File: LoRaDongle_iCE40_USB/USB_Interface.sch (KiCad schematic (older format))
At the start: 25 parts

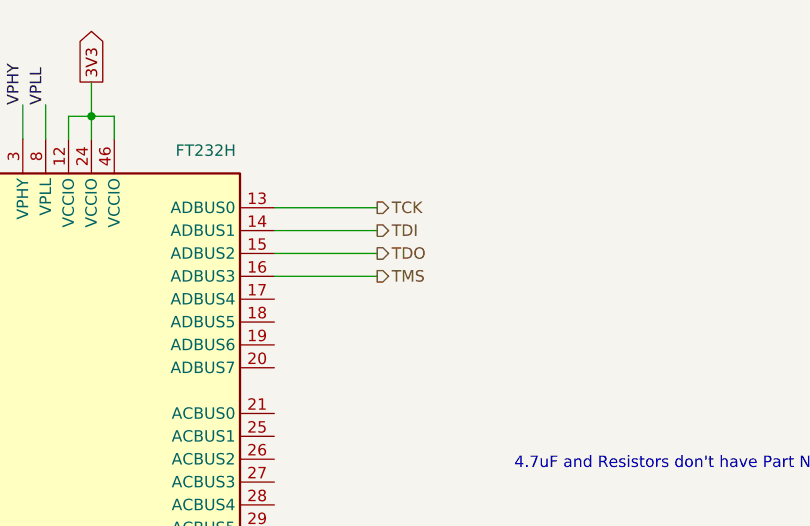
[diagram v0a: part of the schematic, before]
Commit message: initial changes to iCE40UP5k
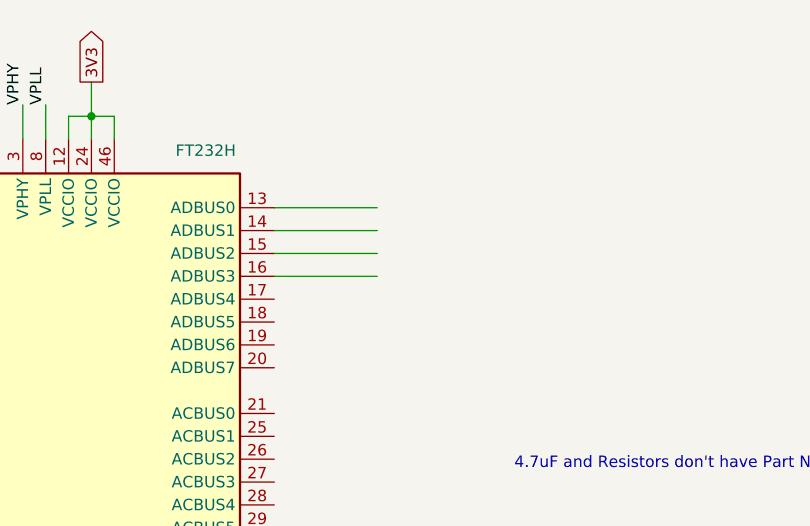
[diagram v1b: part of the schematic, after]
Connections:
- net labels removed: TCK, TDI, TDO, TMS
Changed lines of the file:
@@
 Wire Wire Line
 	7450 1900 7900 1900
-Text HLabel 7900 1600 2    50   Output ~ 0
-TCK
-Text HLabel 7900 1700 2    50   Output ~ 0
-TDI
-Text HLabel 7900 1800 2    50   Output ~ 0
-TDO
-Text HLabel 7900 1900 2    50   Output ~ 0
-TMS
 Text HLabel 5550 2200 0    50   Input ~ 0
 DM

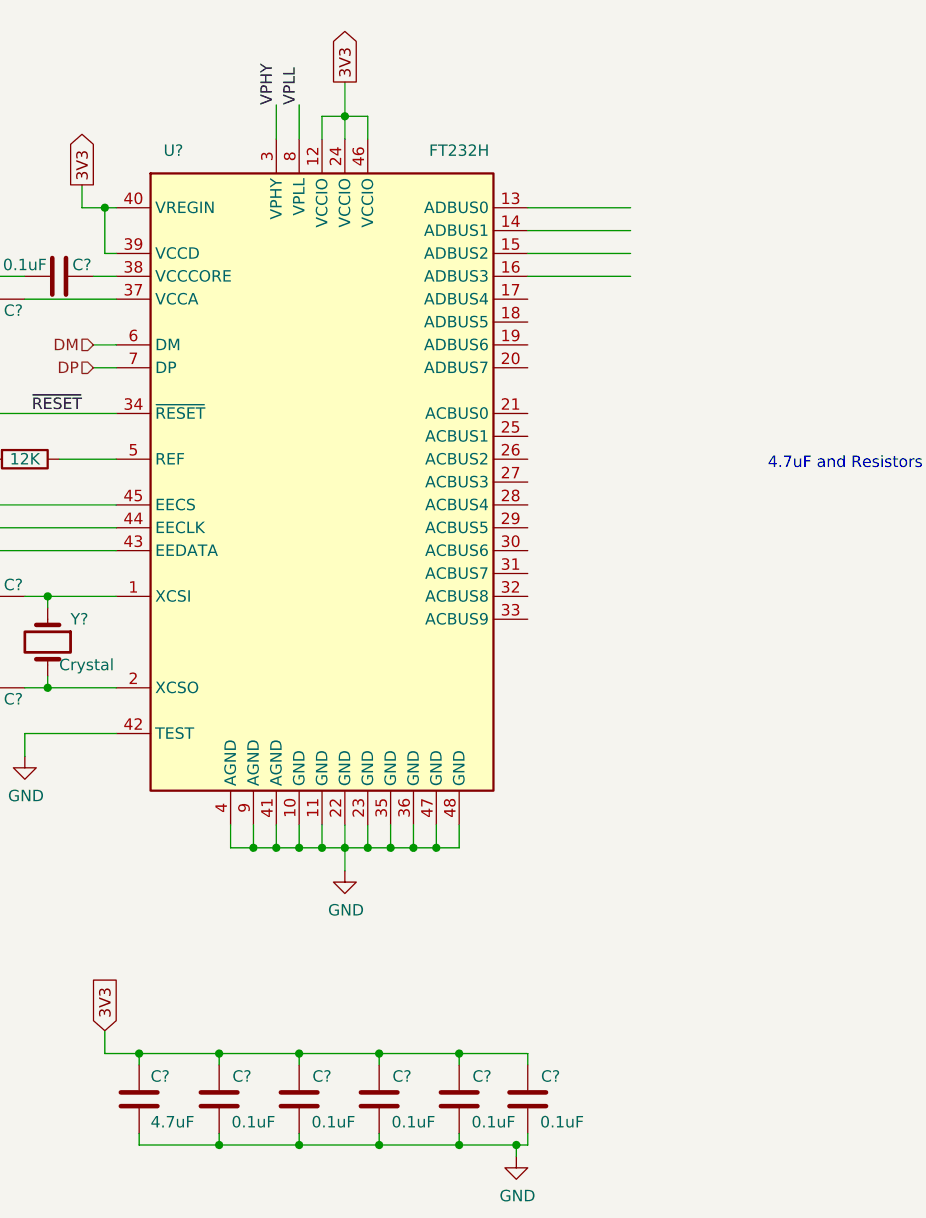
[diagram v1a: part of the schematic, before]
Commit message: changed to sx1261
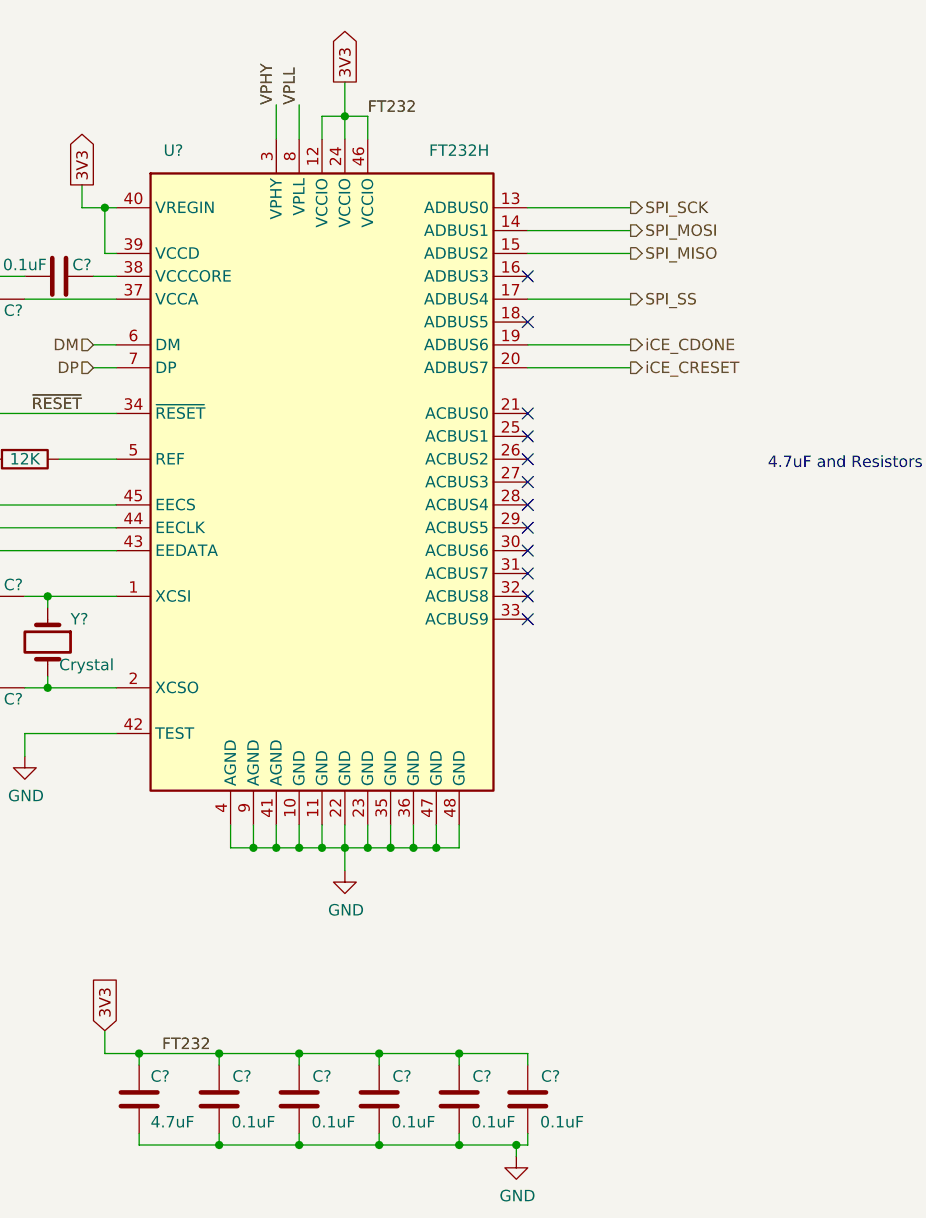
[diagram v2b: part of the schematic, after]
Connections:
- net labels added: FT232, SPI_MISO, SPI_MOSI, SPI_SCK, SPI_SS, iCE_CDONE, iCE_CRESET
- wire segments 129 -> 131
- no-connect marks 0 -> 12
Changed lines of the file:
@@
 $Descr A4 11693 8268
 encoding utf-8
-Sheet 5 5
+Sheet 4 5
 Title ""
 Date ""
@@
 Wire Wire Line
 	7450 1700 7900 1700
-Wire Wire Line
-	7450 1800 7900 1800
-Wire Wire Line
-	7450 1900 7900 1900
 Text HLabel 5550 2200 0    50   Input ~ 0
 DM
@@
 Text Notes 8500 2750 0    50   ~ 0
 4.7uF and Resistors don't have Part Numbers/footprints
+Text HLabel 7900 1600 2    50   Output ~ 0
+SPI_SCK
+Text HLabel 7900 1700 2    50   Output ~ 0
+SPI_MOSI
+Text HLabel 7900 1800 2    50   Output ~ 0
+SPI_MISO
+Text HLabel 7900 2000 2    50   Output ~ 0
+SPI_SS
+Text HLabel 7900 2200 2    50   Output ~ 0
+iCE_CDONE
+Text HLabel 7900 2300 2    50   Output ~ 0
+iCE_CRESET
+Wire Wire Line
+	7450 1800 7900 1800
+Wire Wire Line
+	7450 2000 7900 2000
+Wire Wire Line
+	7450 2200 7900 2200
+Wire Wire Line
+	7450 2300 7900 2300
+NoConn ~ 7450 2100
+NoConn ~ 7450 1900
+NoConn ~ 7450 2500
+NoConn ~ 7450 2600
+NoConn ~ 7450 2700
+NoConn ~ 7450 2800
+NoConn ~ 7450 2900
+NoConn ~ 7450 3000
+NoConn ~ 7450 3100
+NoConn ~ 7450 3200
+NoConn ~ 7450 3300
+NoConn ~ 7450 3400
+Text Label 6750 1200 0    50   ~ 0
+FT232
+Text Label 5850 5300 0    50   ~ 0
+FT232
 $EndSCHEMATC

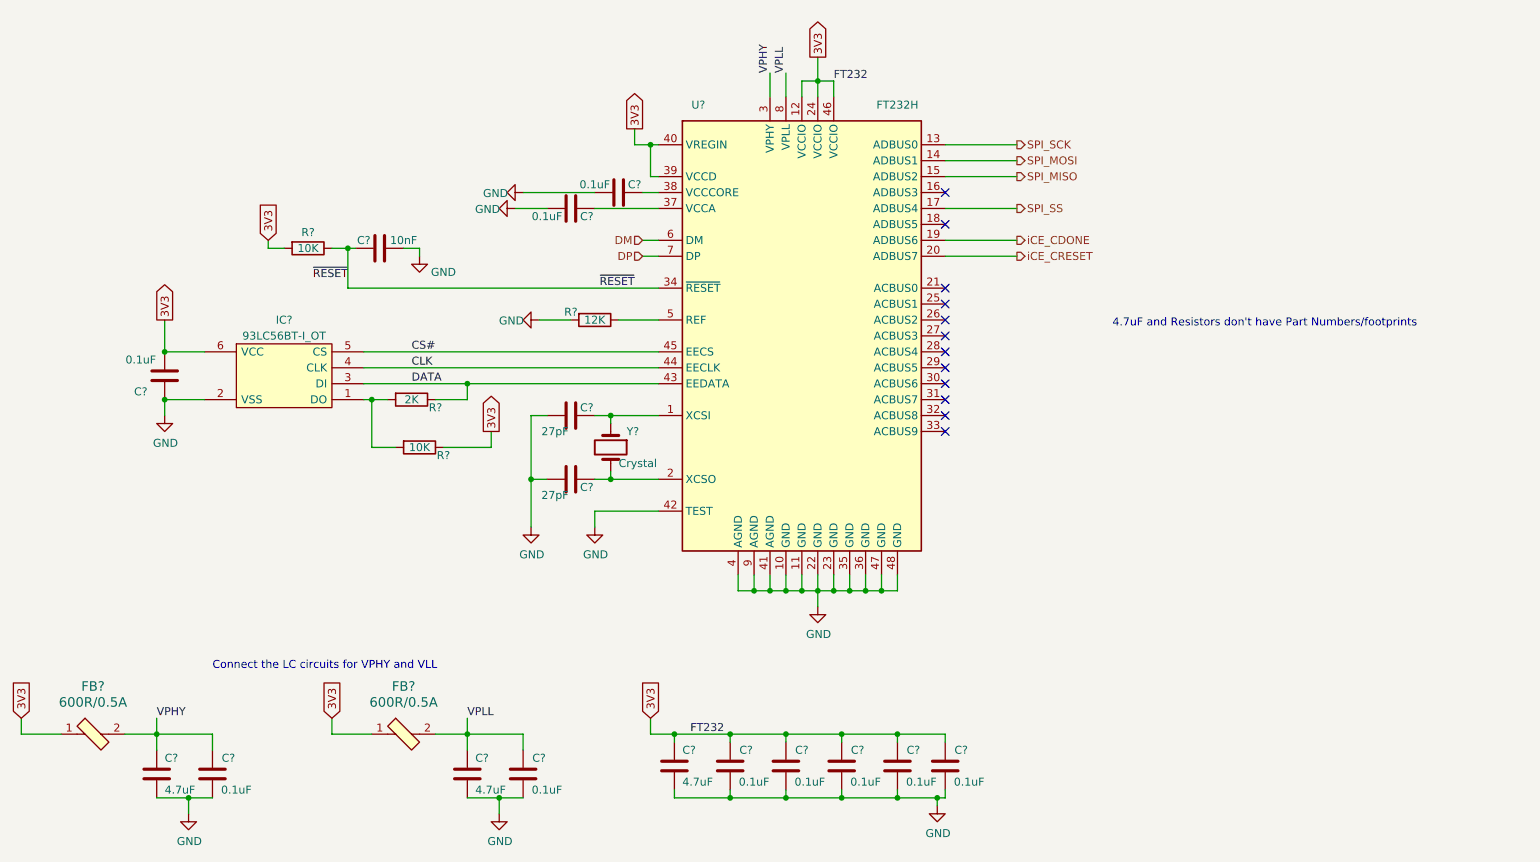
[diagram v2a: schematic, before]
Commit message: added footprints
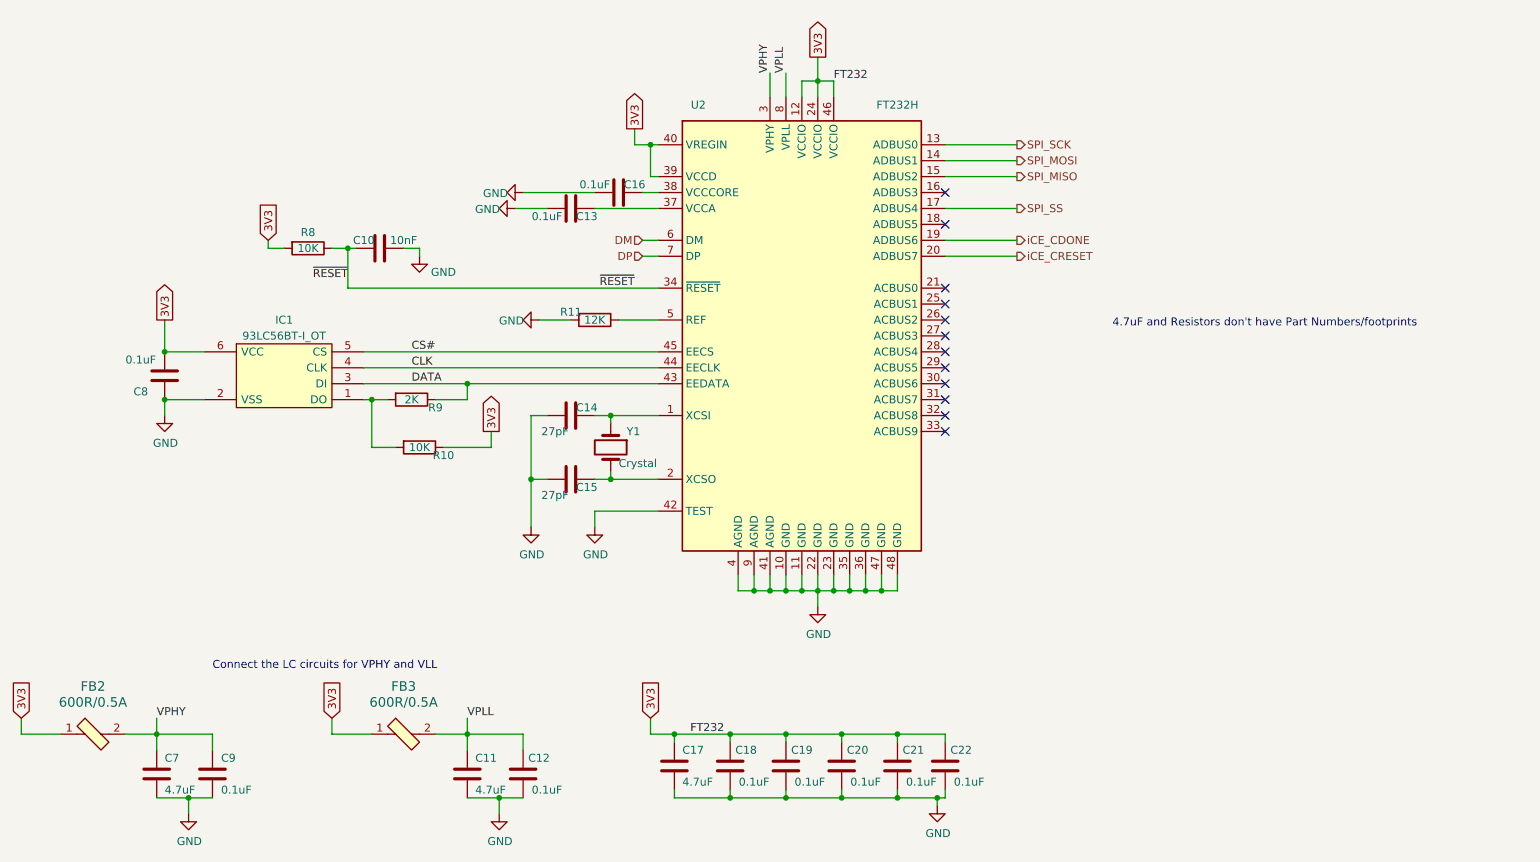
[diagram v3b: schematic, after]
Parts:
- C10: renamed from C?; footprint (none) -> Capacitor_SMD:C_01005_0402Metric; Part Number (none) -> GRM155R71H103KA88J
- C11, C17, C7: renamed from C?; Part Number (none) -> GRM155C80J475MEAAD
- IC1: renamed from IC?; footprint SOT95P270X145-6N -> 93LC56B-I_OT_KiCad:SOT95P270X145-6N
- R10, R11, R8, R9: renamed from R?; footprint (none) -> Resistor_SMD:R_0402_1005Metric
- U2: renamed from U?; footprint (none) -> Package_QFP:LQFP-48_7x7mm_P0.5mm
- gave numbers to parts that had none: 15

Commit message: PCB Layout V01
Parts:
- removed Y1: Crystal, Crystal:Crystal_SMD_3225-4Pin_3.2x2.5mm, symbol Device:Crystal
- added Y1: Crystal_GND24_Small, Crystal:Crystal_SMD_3225-4Pin_3.2x2.5mm, symbol Device:Crystal_GND24_Small
- C10: footprint Capacitor_SMD:C_01005_0402Metric -> Capacitor_SMD:C_0402_1005Metric_Pad0.74x0.62mm_HandSolder
- C11, C14, C15, C17, C7: footprint Capacitor_SMD:C_0603_1608Metric -> Capacitor_SMD:C_0603_1608Metric_Pad1.08x0.95mm_HandSolder
- C12, C13, C16, C18, C19, C20, C21, C22, C8, C9: footprint Capacitor_SMD:C_0402_1005Metric -> Capacitor_SMD:C_0402_1005Metric_Pad0.74x0.62mm_HandSolder
- R10, R11, R8, R9: footprint Resistor_SMD:R_0402_1005Metric -> Resistor_SMD:R_0402_1005Metric_Pad0.72x0.64mm_HandSolder
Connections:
- net GND: now also Y1.2, Y1.4
- net at C14.1, U2.1 (XCSI): now also Y1.1
- net at C15.1, U2.2 (XCSO): now also Y1.3
- net DM renamed USB_D-
- net DP renamed UBS_D+
